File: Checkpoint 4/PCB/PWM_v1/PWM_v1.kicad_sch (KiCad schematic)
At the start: 34 parts, among them J1 Conn_01x02, J2 Conn_01x02, U1 LM7809_TO220, U2 LM393, U3 TL062

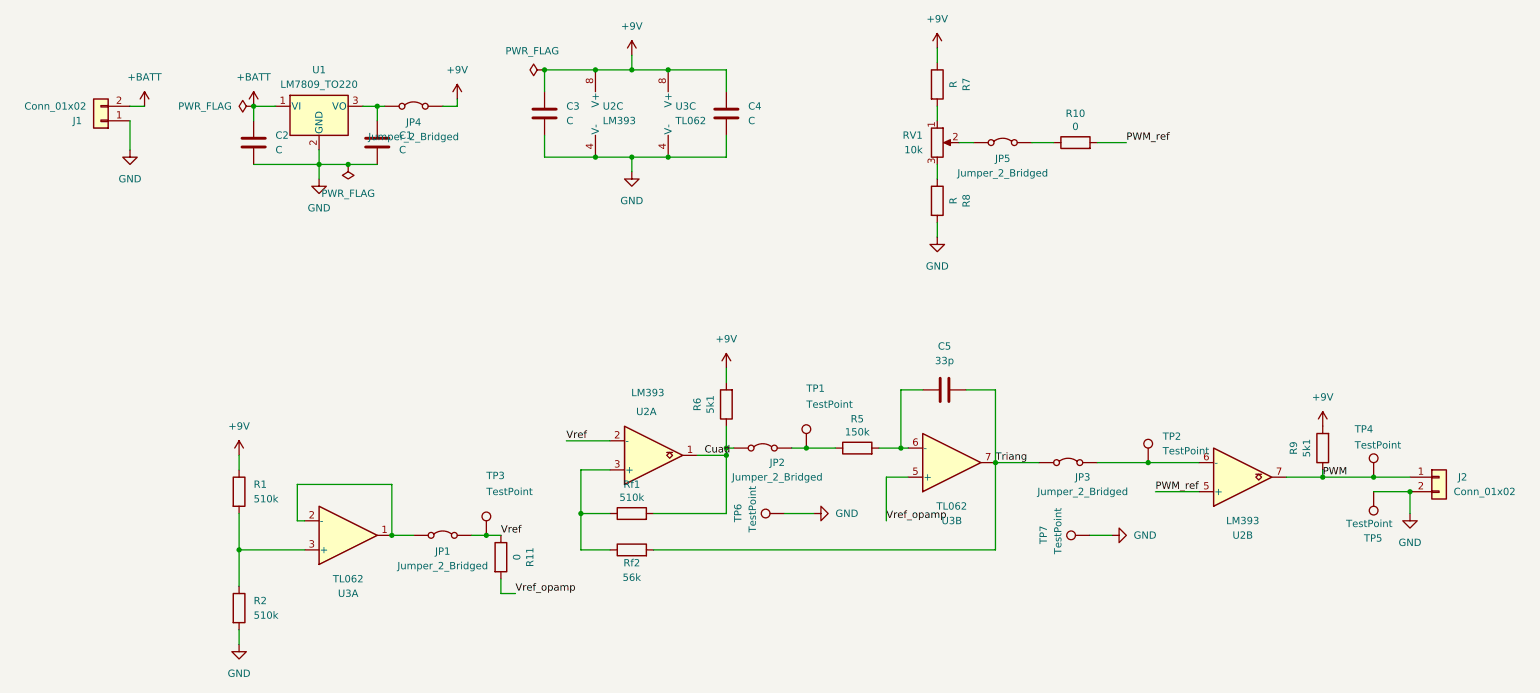
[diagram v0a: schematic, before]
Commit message: Cambié el TL062 por el TL072
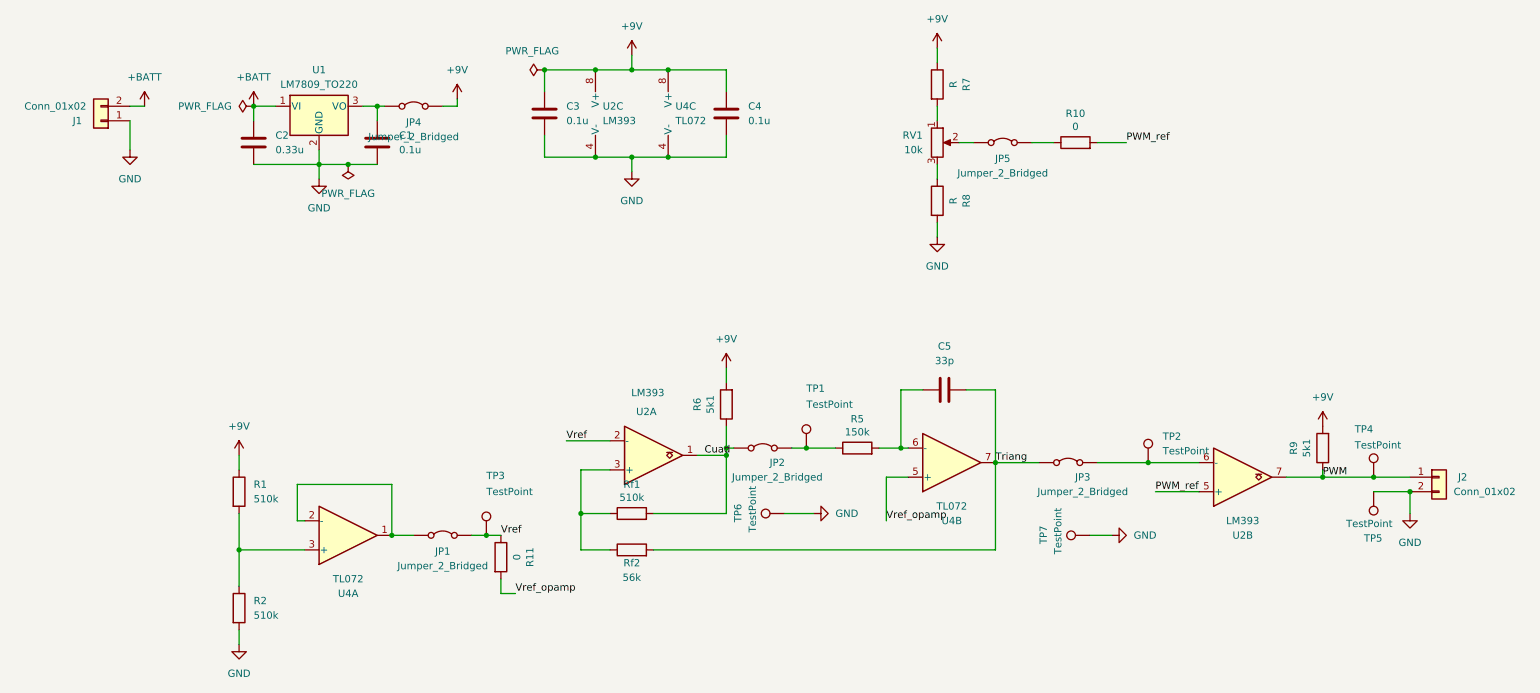
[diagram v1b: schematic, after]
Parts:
- removed U3: TL062, Package_DIP:DIP-8_W7.62mm_Socket_LongPads, symbol Amplifier_Operational:TL062
- added U4: TL072, Package_DIP:DIP-8_W7.62mm_Socket_LongPads, symbol Amplifier_Operational:TL072
- C1, C3, C4: value C -> 0.1u
- C2: value C -> 0.33u
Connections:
- net +9V: now also U4.8 (V+)
- net GND: now also U4.4 (V-)
- net Triang: now also U4.7
- net Vref_opamp: now also U4.5 (+)
- net at JP1.1 (A): now also U4.1, U4.2 (-)
- net at C5.2, R5.2: now also U4.6 (-)
- net at R1.2, R2.1: now also U4.3 (+)

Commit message: lista de materiales
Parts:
- R7, R8: value R -> 10k
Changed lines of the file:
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@@
 			)
 		)
-		(property "Value" "R"
+		(property "Value" "10k"
 			(at 176.784 25.4 90)
 			(show_name no)
@@
 			)
 		)
-		(property "Value" "R"
+		(property "Value" "10k"
 			(at 176.784 45.72 90)
 			(show_name no)

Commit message: cambié un poco la simulación
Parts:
- R1, R2, Rf1: value 510k -> 560k
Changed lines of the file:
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@@
 			)
 		)
-		(property "Value" "510k"
+		(property "Value" "560k"
 			(at 54.61 97.7899 0)
 			(show_name no)
@@
 			)
 		)
-		(property "Value" "510k"
+		(property "Value" "560k"
 			(at 54.61 118.1099 0)
 			(show_name no)
@@
 			)
 		)
-		(property "Value" "510k"
+		(property "Value" "560k"
 			(at 120.65 97.536 90)
 			(show_name no)
